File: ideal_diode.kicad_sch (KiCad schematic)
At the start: 0 parts

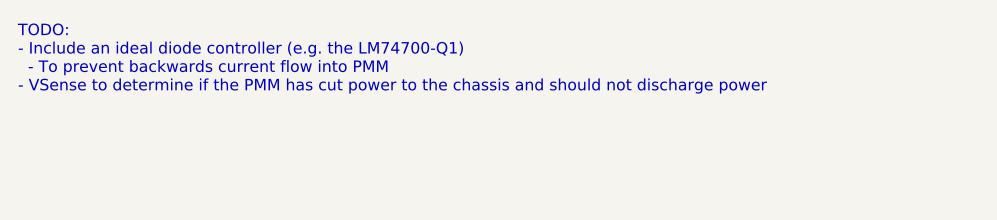
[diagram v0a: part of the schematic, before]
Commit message: Added in & out data from each subsheet
For more details, please contact @leftisttachyon on Discord
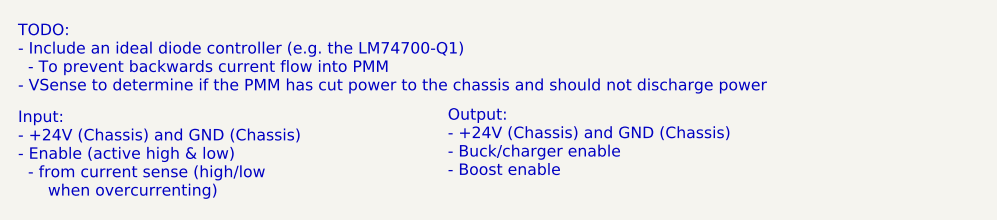
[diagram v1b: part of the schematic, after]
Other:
- note added: "Input: - +24V (Chassis) and GND (Chassis) - Enable (active high & low) - from current sense (high/low when overcurrenting)"
- note added: "Output: - +24V (Chassis) and GND (Chassis) - Buck/charger enable - Boost enable"
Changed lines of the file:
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@@
 	(generator_version "8.0")
 	(paper "A4")
+	(text "Input:\n- +24V (Chassis) and GND (Chassis)\n- Enable (active high & low)\n  - from current sense (high/low \n      when overcurrenting)"
+		(exclude_from_sim no)
+		(at 105.664 104.902 0)
+		(effects
+			(font
+				(size 1.27 1.27)
+			)
+			(justify left top)
+		)
+	)
+	(text "Output:\n- +24V (Chassis) and GND (Chassis)\n- Buck/charger enable\n- Boost enable"
+		(exclude_from_sim no)
+		(at 153.416 104.648 0)
+		(effects
+			(font
+				(size 1.27 1.27)
+			)
+			(justify left top)
+		)
+	)
 	(text "TODO:\n- Include an ideal diode controller (e.g. the LM74700-Q1)\n  - To prevent backwards current flow into PMM\n- VSense to determine if the PMM has cut power to the chassis and should not discharge power"
 		(exclude_from_sim no)

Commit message: Completed first version of housekeeping supplies
+5V and +3V3 from mini PC +24V
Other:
- company: (none) -> UT Robomaster
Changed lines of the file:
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@@
 	(generator_version "8.0")
 	(paper "A4")
+	(title_block
+		(date "2024-11-15")
+		(rev "1")
+		(company "UT Robomaster")
+	)
 	(text "Input:\n- +24V (Chassis) and GND (Chassis)\n- Enable (active high & low)\n  - from current sense (high/low \n      when overcurrenting)"
 		(exclude_from_sim no)

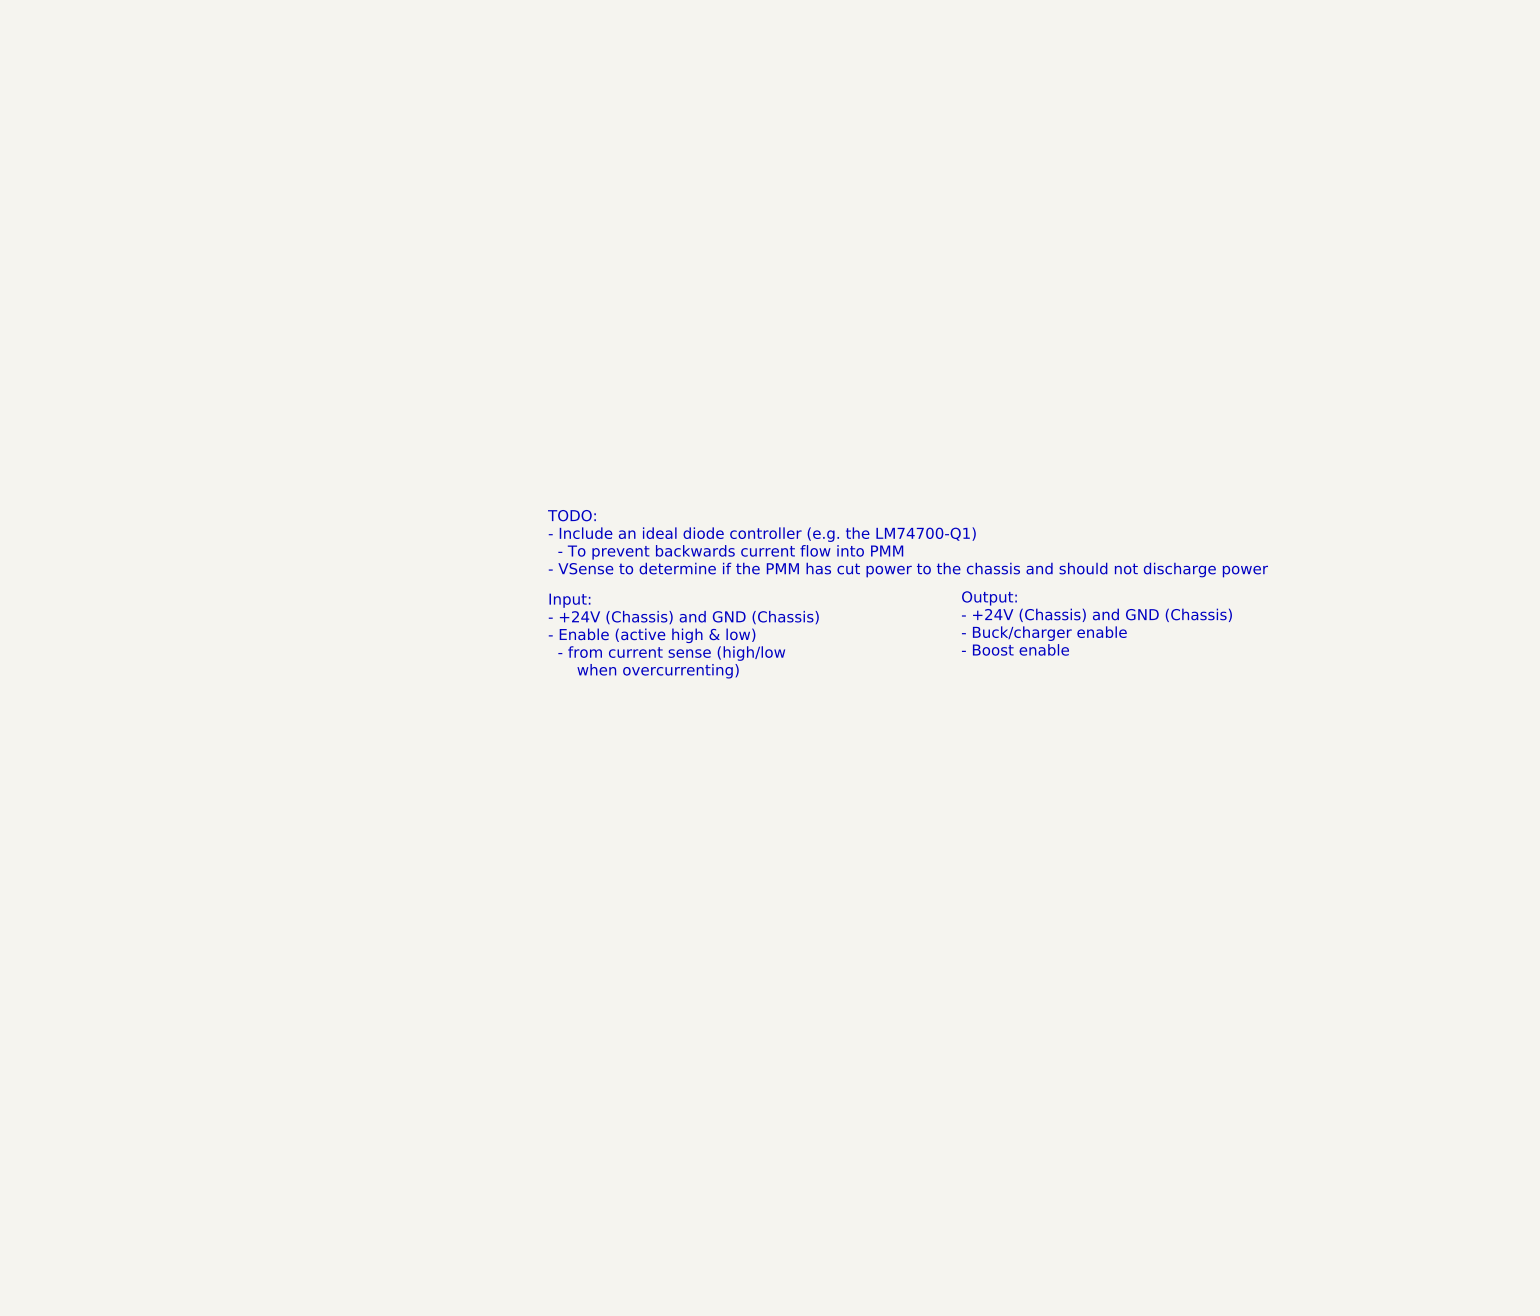
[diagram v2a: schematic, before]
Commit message: Selected an ideal diode
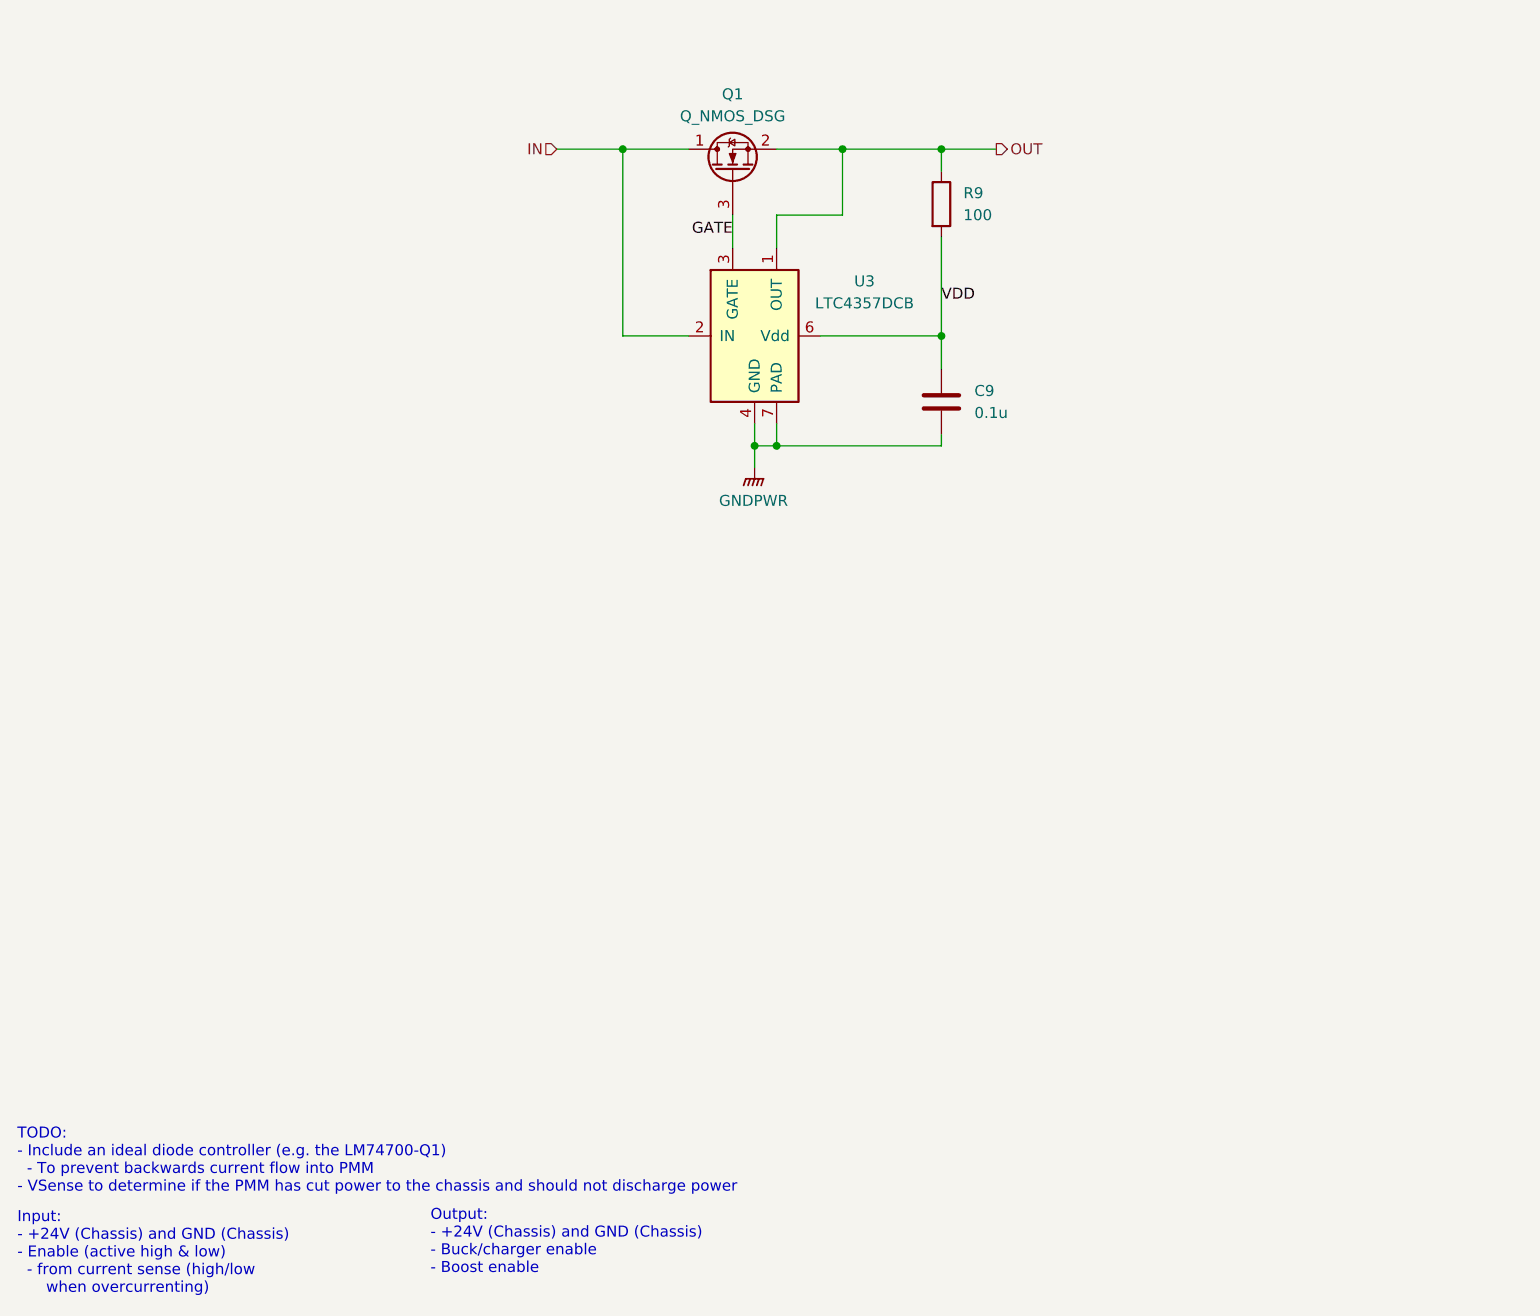
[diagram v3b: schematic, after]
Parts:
- added C9: 0.1u, Capacitor_SMD:C_0603_1608Metric_Pad1.08x0.95mm_HandSolder, symbol Device:C
- added Q1: Q_NMOS_DSG, symbol Device:Q_NMOS_DSG
- added R9: 100, Resistor_SMD:R_0603_1608Metric_Pad0.98x0.95mm_HandSolder, symbol Device:R
- added U3: LTC4357DCB, Package_DFN_QFN:DFN-6-1EP_3x2mm_P0.5mm_EP1.65x1.35mm, symbol Power_Management:LTC4357DCB
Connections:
- new net GATE: Q1.3 (G), U3.3 (GATE)
- new net GNDPWR: C9.2, U3.4 (GND), U3.7 (PAD)
- new net IN: Q1.1 (D), U3.2 (IN)
- new net OUT: Q1.2 (S), R9.1, U3.1 (OUT)
- new net VDD: C9.1, R9.2, U3.6 (Vdd)

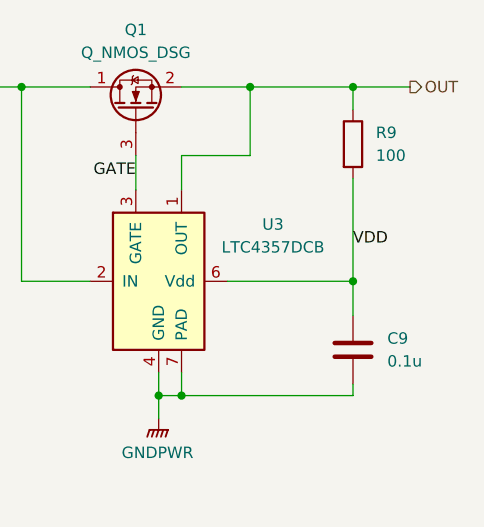
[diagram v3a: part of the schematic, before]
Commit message: Selected components for ideal diode and DACs
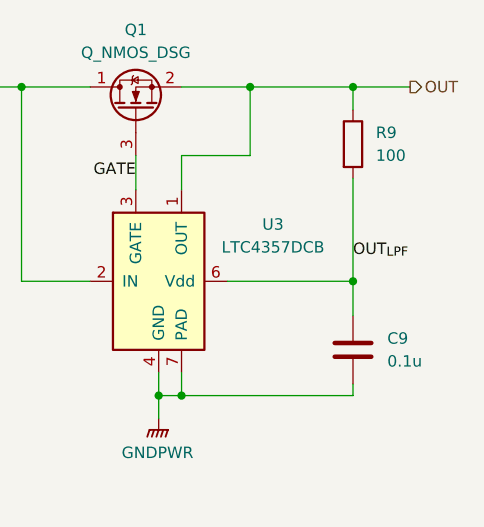
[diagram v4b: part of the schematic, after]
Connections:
- net VDD renamed OUT_{LPF}
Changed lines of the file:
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@@
 		)
 	)
-	(label "VDD"
-		(at 151.13 71.12 0)
+	(label "OUT_{LPF}"
+		(at 151.13 72.39 0)
 		(fields_autoplaced yes)
 		(effects

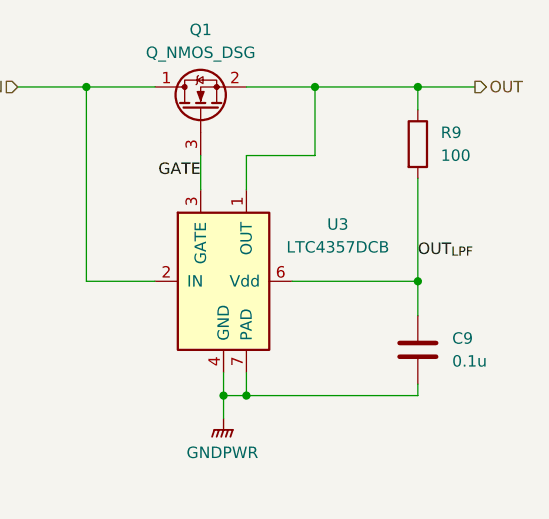
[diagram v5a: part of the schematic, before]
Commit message: Updating symbol library + passing some ERC tests
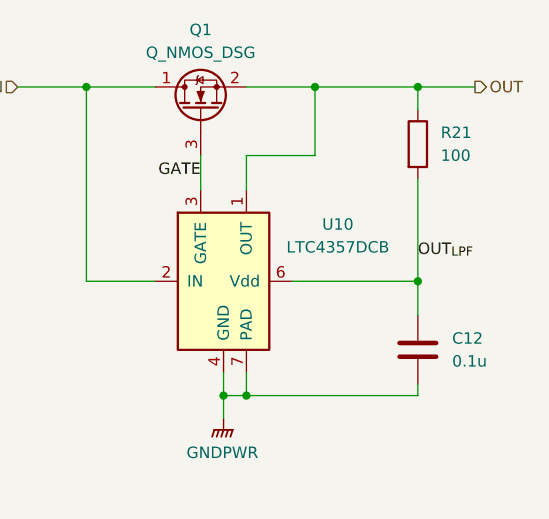
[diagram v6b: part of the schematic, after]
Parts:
- renumbered C9 to C12, R9 to R21, U3 to U10
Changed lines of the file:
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@@
 		(dnp no)
 		(fields_autoplaced yes)
-		(property "Reference" "C9"
+		(property "Reference" "C12"
 			(at 154.94 81.2799 0)
 			(effects
@@
 			(project ""
 				(path "/6197145b-e7d4-44cc-9d90-537b6501bf60/f28a7bbd-a217-4ab0-a73c-be6ca56ea928"
-					(reference "C9")
+					(reference "C12")
 					(unit 1)
 				)
@@
 		(dnp no)
 		(fields_autoplaced yes)
-		(property "Reference" "R9"
+		(property "Reference" "R21"
 			(at 153.67 58.4199 0)
 			(effects
@@
 			(project ""
 				(path "/6197145b-e7d4-44cc-9d90-537b6501bf60/f28a7bbd-a217-4ab0-a73c-be6ca56ea928"
-					(reference "R9")
+					(reference "R21")
 					(unit 1)
 				)
@@
 		(dnp no)
 		(fields_autoplaced yes)
-		(property "Reference" "#PWR07"
+		(property "Reference" "#PWR046"
 			(at 129.54 95.25 0)
 			(effects
@@
 			(project ""
 				(path "/6197145b-e7d4-44cc-9d90-537b6501bf60/f28a7bbd-a217-4ab0-a73c-be6ca56ea928"
-					(reference "#PWR07")
+					(reference "#PWR046")
 					(unit 1)
 				)
@@
 		(dnp no)
 		(fields_autoplaced yes)
-		(property "Reference" "U3"
+		(property "Reference" "U10"
 			(at 142.24 68.6114 0)
 			(effects
@@
 			(project ""
 				(path "/6197145b-e7d4-44cc-9d90-537b6501bf60/f28a7bbd-a217-4ab0-a73c-be6ca56ea928"
-					(reference "U3")
-					(unit 1)
-				)
+					(reference "U10")
+					(unit 1)
+				)

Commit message: Add input resistor divider to battery voltage ADC
+ renumbered components
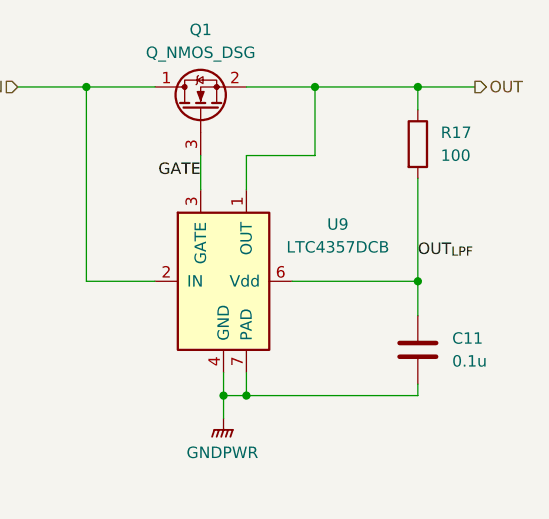
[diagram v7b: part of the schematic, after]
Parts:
- renumbered C12 to C11, R21 to R17, U10 to U9
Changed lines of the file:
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@@
 		(dnp no)
 		(fields_autoplaced yes)
-		(property "Reference" "C12"
+		(property "Reference" "C11"
 			(at 154.94 81.2799 0)
 			(effects
@@
 			(project ""
 				(path "/6197145b-e7d4-44cc-9d90-537b6501bf60/f28a7bbd-a217-4ab0-a73c-be6ca56ea928"
-					(reference "C12")
+					(reference "C11")
 					(unit 1)
 				)
@@
 		(dnp no)
 		(fields_autoplaced yes)
-		(property "Reference" "R21"
+		(property "Reference" "R17"
 			(at 153.67 58.4199 0)
 			(effects
@@
 			(project ""
 				(path "/6197145b-e7d4-44cc-9d90-537b6501bf60/f28a7bbd-a217-4ab0-a73c-be6ca56ea928"
-					(reference "R21")
+					(reference "R17")
 					(unit 1)
 				)
@@
 		(dnp no)
 		(fields_autoplaced yes)
-		(property "Reference" "#PWR046"
+		(property "Reference" "#PWR044"
 			(at 129.54 95.25 0)
 			(effects
@@
 			(project ""
 				(path "/6197145b-e7d4-44cc-9d90-537b6501bf60/f28a7bbd-a217-4ab0-a73c-be6ca56ea928"
-					(reference "#PWR046")
+					(reference "#PWR044")
 					(unit 1)
 				)
@@
 		(dnp no)
 		(fields_autoplaced yes)
-		(property "Reference" "U10"
+		(property "Reference" "U9"
 			(at 142.24 68.6114 0)
 			(effects
@@
 			(project ""
 				(path "/6197145b-e7d4-44cc-9d90-537b6501bf60/f28a7bbd-a217-4ab0-a73c-be6ca56ea928"
-					(reference "U10")
-					(unit 1)
-				)
+					(reference "U9")
+					(unit 1)
+				)
